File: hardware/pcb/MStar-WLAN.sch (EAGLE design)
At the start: 43 parts, among them J1 Kobiconn 154-UL6661, J3 DX07S016JA1R1500, Q1 VP2106, Q2 TN0606

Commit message: hardware, configurable hostname
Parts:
- renumbered BZW04-17B to BZW04-28B
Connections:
- net N$6 renamed CC2
- net N$7 renamed CC1
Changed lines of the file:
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@@
 <grid distance="0.1" unitdist="inch" unit="inch" style="lines" multiple="1" display="no" altdistance="0.01" altunitdist="inch" altunit="inch"/>
 <layers>
-<layer number="1" name="Top" color="4" fill="1" visible="yes" active="no"/>
-<layer number="16" name="Bottom" color="1" fill="1" visible="yes" active="no"/>
-<layer number="17" name="Pads" color="2" fill="1" visible="yes" active="no"/>
-<layer number="18" name="Vias" color="2" fill="1" visible="yes" active="no"/>
-<layer number="19" name="Unrouted" color="6" fill="1" visible="yes" active="no"/>
-<layer number="20" name="Dimension" color="15" fill="1" visible="yes" active="no"/>
-<layer number="21" name="tPlace" color="7" fill="1" visible="yes" active="no"/>
-<layer number="22" name="bPlace" color="7" fill="1" visible="yes" active="no"/>
-<layer number="23" name="tOrigins" color="15" fill="1" visible="yes" active="no"/>
-<layer number="24" name="bOrigins" color="15" fill="1" visible="yes" active="no"/>
-<layer number="25" name="tNames" color="7" fill="1" visible="yes" active="no"/>
-<layer number="26" name="bNames" color="7" fill="1" visible="yes" active="no"/>
-<layer number="27" name="tValues" color="7" fill="1" visible="yes" active="no"/>
-<layer number="28" name="bValues" color="7" fill="1" visible="yes" active="no"/>
+<layer number="1" name="Top" color="4" fill="1" visible="no" active="no"/>
+<layer number="16" name="Bottom" color="1" fill="1" visible="no" active="no"/>
+<layer number="17" name="Pads" color="2" fill="1" visible="no" active="no"/>
+<layer number="18" name="Vias" color="2" fill="1" visible="no" active="no"/>
+<layer number="19" name="Unrouted" color="6" fill="1" visible="no" active="no"/>
+<layer number="20" name="Dimension" color="15" fill="1" visible="no" active="no"/>
+<layer number="21" name="tPlace" color="7" fill="1" visible="no" active="no"/>
+<layer number="22" name="bPlace" color="7" fill="1" visible="no" active="no"/>
+<layer number="23" name="tOrigins" color="15" fill="1" visible="no" active="no"/>
+<layer number="24" name="bOrigins" color="15" fill="1" visible="no" active="no"/>
+<layer number="25" name="tNames" color="7" fill="1" visible="no" active="no"/>
+<layer number="26" name="bNames" color="7" fill="1" visible="no" active="no"/>
+<layer number="27" name="tValues" color="7" fill="1" visible="no" active="no"/>
+<layer number="28" name="bValues" color="7" fill="1" visible="no" active="no"/>
 <layer number="29" name="tStop" color="7" fill="3" visible="no" active="no"/>
 <layer number="30" name="bStop" color="7" fill="6" visible="no" active="no"/>
@@
 <layer number="35" name="tGlue" color="7" fill="4" visible="no" active="no"/>
 <layer number="36" name="bGlue" color="7" fill="5" visible="no" active="no"/>
-<layer number="37" name="tTest" color="7" fill="1" visible="yes" active="no"/>
-<layer number="38" name="bTest" color="7" fill="1" visible="yes" active="no"/>
+<layer number="37" name="tTest" color="7" fill="1" visible="no" active="no"/>
+<layer number="38" name="bTest" color="7" fill="1" visible="no" active="no"/>
 <layer number="39" name="tKeepout" color="4" fill="11" visible="no" active="no"/>
 <layer number="40" name="bKeepout" color="1" fill="11" visible="no" active="no"/>
@@
 <layer number="44" name="Drills" color="7" fill="1" visible="no" active="no"/>
 <layer number="45" name="Holes" color="7" fill="1" visible="no" active="no"/>
-<layer number="46" name="Milling" color="3" fill="1" visible="yes" active="no"/>
-<layer number="47" name="Measures" color="7" fill="1" visible="yes" active="no"/>
-<layer number="48" name="Document" color="7" fill="1" visible="yes" active="no"/>
-<layer number="49" name="Reference" color="7" fill="1" visible="yes" active="no"/>
-<layer number="50" name="dxf" color="7" fill="1" visible="yes" active="no"/>
-<layer number="51" name="tDocu" color="7" fill="1" visible="yes" active="no"/>
-<layer number="52" name="bDocu" color="7" fill="1" visible="yes" active="no"/>
-<layer number="53" name="tGND_GNDA" color="7" fill="9" visible="yes" active="no"/>
-<layer number="54" name="bGND_GNDA" color="1" fill="9" visible="yes" active="no"/>
-<layer number="56" name="wert" color="7" fill="1" visible="yes" active="no"/>
-<layer number="57" name="tCAD" color="7" fill="1" visible="yes" active="no"/>
-<layer number="59" name="tCarbon" color="7" fill="1" visible="yes" active="no"/>
-<layer number="60" name="bCarbon" color="7" fill="1" visible="yes" active="no"/>
+<layer number="46" name="Milling" color="3" fill="1" visible="no" active="no"/>
+<layer number="47" name="Measures" color="7" fill="1" visible="no" active="no"/>
+<layer number="48" name="Document" color="7" fill="1" visible="no" active="no"/>
+<layer number="49" name="Reference" color="7" fill="1" visible="no" active="no"/>
+<layer number="50" name="dxf" color="7" fill="1" visible="no" active="no"/>
+<layer number="51" name="tDocu" color="7" fill="1" visible="no" active="no"/>
+<layer number="52" name="bDocu" color="7" fill="1" visible="no" active="no"/>
+<layer number="53" name="tGND_GNDA" color="7" fill="9" visible="no" active="no"/>
+<layer number="54" name="bGND_GNDA" color="1" fill="9" visible="no" active="no"/>
+<layer number="56" name="wert" color="7" fill="1" visible="no" active="no"/>
+<layer number="57" name="tCAD" color="7" fill="1" visible="no" active="no"/>
+<layer number="59" name="tCarbon" color="7" fill="1" visible="no" active="no"/>
+<layer number="60" name="bCarbon" color="7" fill="1" visible="no" active="no"/>
 <layer number="88" name="SimResults" color="9" fill="1" visible="no" active="yes"/>
 <layer number="89" name="SimProbes" color="9" fill="1" visible="no" active="yes"/>
@@
 <part name="VR1" library="MStar-WLAN" deviceset="VREG" device="-OKI-78SR-3.3/1.5-W36"/>
 <part name="SDCARD0" library="MStar-WLAN" deviceset="DM3BT-DSF-PEJS" device=""/>
-<part name="BZW04-17B" library="MStar-WLAN" deviceset="TVS-" device=""/>
+<part name="BZW04-28B" library="MStar-WLAN" deviceset="TVS-" device=""/>
 <part name="32768HZ" library="MStar-WLAN" deviceset="MCS10B" device=""/>
 <part name="VR2" library="MStar-WLAN" deviceset="VREG" device="-TS1117CW-3V3" value="LDL1117S33"/>
@@
 <attribute name="VALUE" x="165.1" y="-15.24" size="1.778" layer="96" ratio="12" rot="MR0"/>
 </instance>
-<instance part="BZW04-17B" gate="G$1" x="63.5" y="15.24" smashed="yes" rot="R90">
+<instance part="BZW04-28B" gate="G$1" x="63.5" y="15.24" smashed="yes" rot="R90">
 <attribute name="NAME" x="66.675" y="10.795" size="1.778" layer="95" rot="R90"/>
 </instance>
@@
 <wire x1="68.58" y1="76.2" x2="68.58" y2="81.28" width="0.1524" layer="91"/>
 <junction x="68.58" y="81.28"/>
-<pinref part="BZW04-17B" gate="G$1" pin="2"/>
+<pinref part="BZW04-28B" gate="G$1" pin="2"/>
 <wire x1="63.5" y1="81.28" x2="63.5" y2="17.78" width="0.1524" layer="91"/>
 <junction x="63.5" y="81.28"/>
@@
 <junction x="68.58" y="-10.16"/>
 <wire x1="63.5" y1="-10.16" x2="68.58" y2="-10.16" width="0.1524" layer="91"/>
-<pinref part="BZW04-17B" gate="G$1" pin="1"/>
+<pinref part="BZW04-28B" gate="G$1" pin="1"/>
 <wire x1="63.5" y1="10.16" x2="63.5" y2="-10.16" width="0.1524" layer="91"/>
 <junction x="63.5" y="-10.16"/>
@@
 </segment>
 </net>
-<net name="N$6" class="0">
+<net name="CC2" class="0">
 <segment>
 <pinref part="J3" gate="G$1" pin="CC2"/>
@@
 </segment>
 </net>
-<net name="N$7" class="0">
+<net name="CC1" class="0">
 <segment>
 <pinref part="J3" gate="G$1" pin="CC1"/>

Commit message: Hardware update
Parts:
- removed BZW04-28B: TVS-, MStar-WLAN:TVS-
- added D3: BZW04-33, diode:ZPY
- BOOT, RESET: value (none) -> PTS645SM432LFS
- C12: device rcl:CPOL-USE5-8.5 -> rcl:CPOL-USE5-6
- MBUS: value (none) -> Green
- WLAN: value (none) -> Red
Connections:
- net /MBUS: now also D3.C; no longer BZW04-28B.2
- net GND: now also D3.A; no longer BZW04-28B.1
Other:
- note added: "MStar-WLAN 2020.11 mjs"
- note removed: "MStar-WLAN 2020.10 mjs"
- moved on the sheet: C10

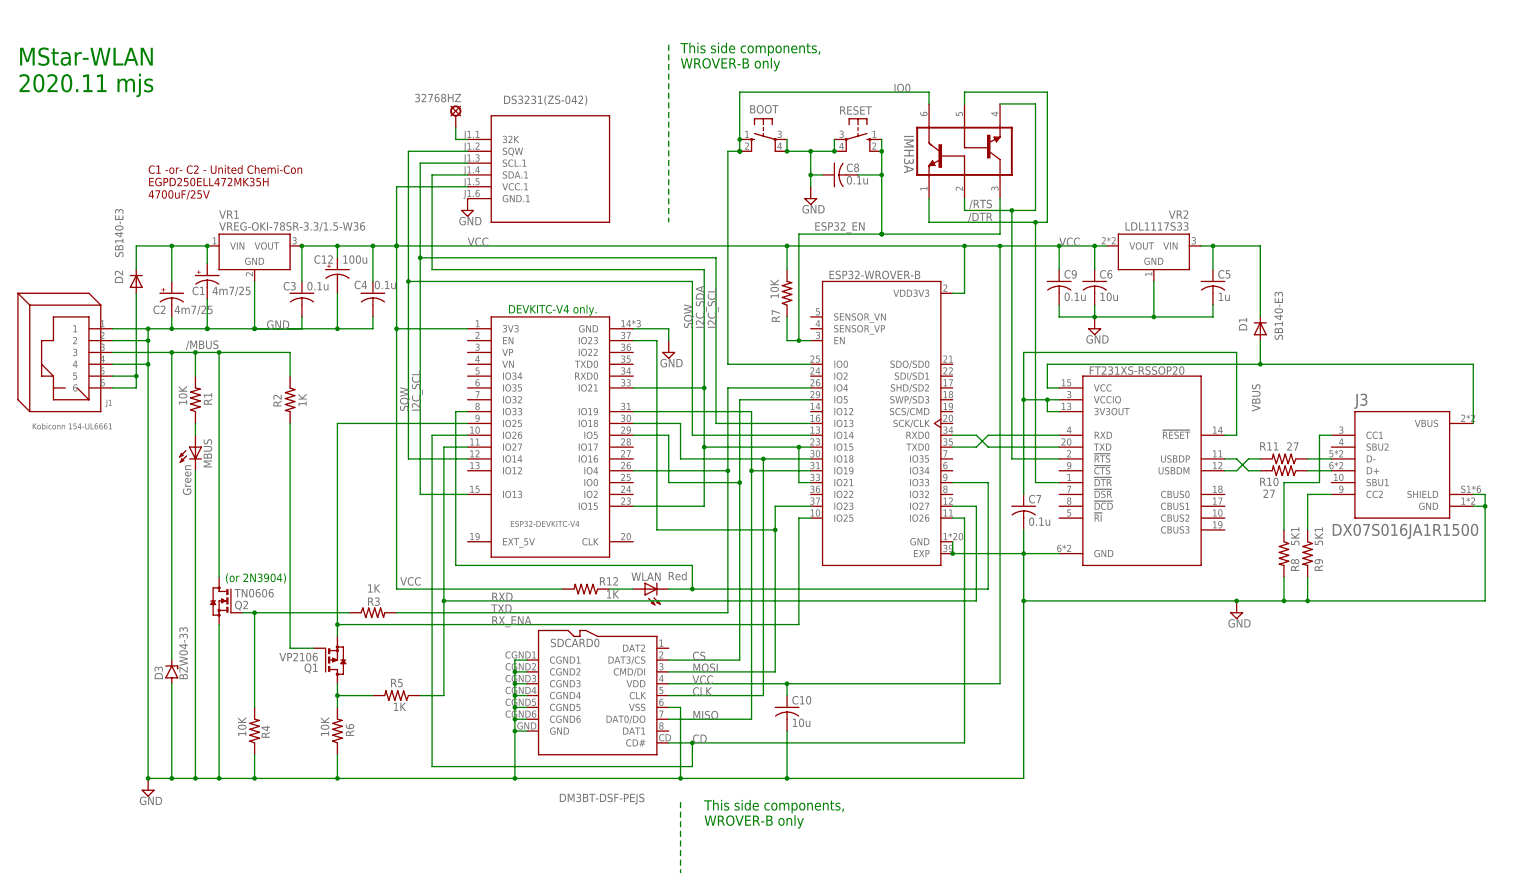
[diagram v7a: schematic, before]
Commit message: Hardware, charting, much more
Hardware updated for USB-C and to support Devkit-C.
Charting using an RRD database and JavascriptRRD / FLOT.
Show temperature in C or F on /status page.
Configurable logging period for traditional log.
Lots of bug fixes and tweaks, especially in Modbus.
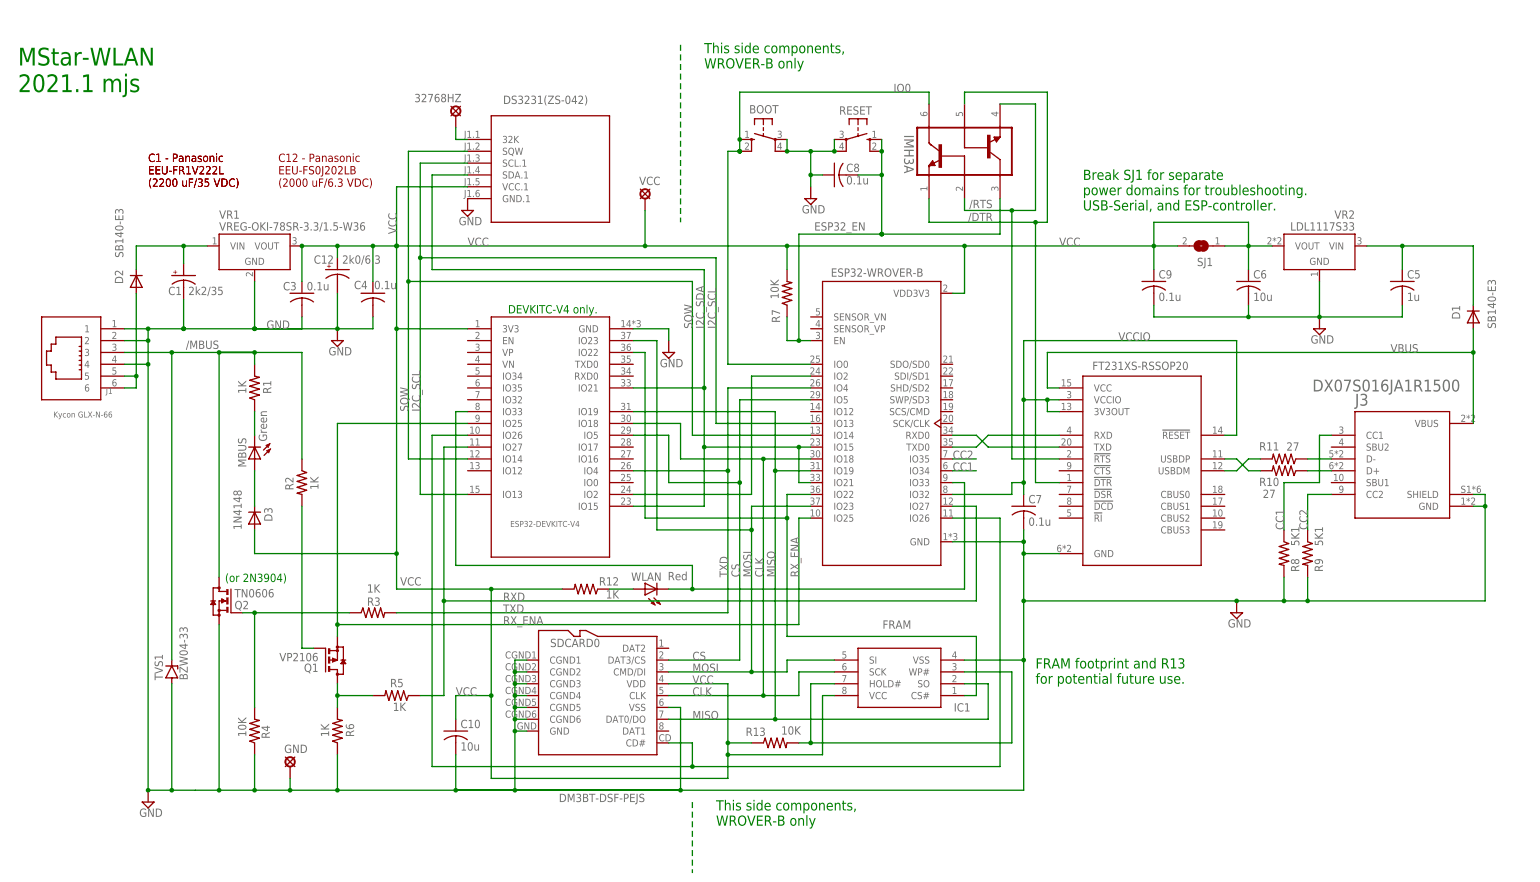
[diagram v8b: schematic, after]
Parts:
- removed C2: 4m7/25, MStar-WLAN:CPOL-USE5-4
- added GND, VCC: MCS10B, MStar-WLAN:MCS10B
- added IC1: FRAM, MStar-WLAN:MR45V100AMAZAATLSO8M
- added R13: 10K, rcl:R-US_R1206
- added SJ1: (no value), jumper:SJ
- added TVS1: BZW04-33, diode:ZPY
- C1: value 4m7/25 -> 2k2/35
- C12: value 100u -> 2k0/6.3
- D3: value BZW04-33 -> 1N4148; device diode:ZPY -> MStar-WLAN:1N4148DO35-7
- J1: value Kobiconn 154-UL6661 -> Kycon GLX-N-66; device MStar-WLAN:RJ12 -> MStar-WLAN:6P6C
- R1, R6: value 10K -> 1K
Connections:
- removed net N$15: C7.1, FT231XS.!RESET, FT231XS.3V3OUT, FT231XS.VCCIO
- new net N$6: ESP32-WROVER-B.IO22, IC1.CS#, U$1.IO22
- new net N$7: IC1.HOLD#, IC1.WP#, R13.2
- new net N$8: D3.C, MBUS.A
- new net N$9: ESP32-WROVER-B.IO2, U$1.IO2
- new net VCCIO: C7.1, ESP32-WROVER-B.IO32, FT231XS.!RESET, FT231XS.3V3OUT, FT231XS.VCCIO
- net /MBUS: now also TVS1.C; no longer D3.C
- net CC1: now also ESP32-WROVER-B.IO34
- net CC2: now also ESP32-WROVER-B.IO35
- net CLK: now also IC1.SCK
- net GND: now also GND.MP, IC1.VSS, TVS1.A; no longer C2.-, D3.A, ESP32-WROVER-B.EXP, MBUS.C
- net MISO: now also IC1.SO
- net MOSI: now also IC1.SI
- net N$1: now also MBUS.C; no longer MBUS.A
- net RAW12: no longer C2.+
- net VCC: now also D3.A, IC1.VCC, R13.1, SJ1.1, SJ1.2, VCC.MP
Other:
- note added: "Break SJ1 for separate power domains for troubleshooting. USB-Serial, and ESP-controller."
- note added: "C1 - Panasonic EEU-FR1V222L (2200 uF/35 VDC)"
- note added: "C12 - Panasonic EEU-FS0J202LB (2000 uF/6.3 VDC)"
- note added: "FRAM footprint and R13 for potential future use."
- note added: "MStar-WLAN 2021.1 mjs"
- note removed: "C1 -or- C2 - United Chemi-Con EGPD250ELL472MK35H 4700uF/25V"
- note removed: "MStar-WLAN 2020.11 mjs"
- moved on the sheet: C1, C10, C5, C6, C9, D1, MBUS, R1, R2, VR2
